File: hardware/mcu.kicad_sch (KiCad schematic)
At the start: 38 parts, among them J1 USB-C, SW3 RUN, SW4 BOOTSEL, U20 RP2350B, U21 W25Q128JVSIQ, U22 APS6404L-3SQR-SN, Y1 12MHz

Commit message: Hand-finish the last eight connections: fully routed, zero DRC errors
finish_route.py adds plane vias, clearance-checked stubs and single-layer
A* routing. Five signals run partly on the +3V3 plane layer (In2). SD_MISO
moves from GP36 to GP32 (both SPI0 RX) because the GP36 pad has no exit.
Schematic, GPIO table and README updated.

Co-Authored-By: Claude Fable 5.1 <noreply@anthropic.com>
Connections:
- net SD_MISO: now also U20.40 (GPIO32); no longer U20.45 (GPIO36)
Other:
- note added: "RP2350B core per the RP2350 hardware design guide. GPIO map: docs/v3-architecture.md section 7. GP31, GP33-GP36 spare."
- note removed: "RP2350B core per the RP2350 hardware design guide. GPIO map: docs/v3-architecture.md section 7. GP31-GP35 spare."
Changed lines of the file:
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@@
   (paper "A3")
   (title_block (title "TS-Pico v3: RP2350B Core") (rev "0.1") (company "Timex/Sinclair Online User Group"))
-  (text "RP2350B core per the RP2350 hardware design guide. GPIO map: docs/v3-architecture.md section 7. GP31-GP35 spare." (exclude_from_sim no) (at 20 285 0) (effects (font (size 2.5 2.5)) (justify left bottom)))
+  (text "RP2350B core per the RP2350 hardware design guide. GPIO map: docs/v3-architecture.md section 7. GP31, GP33-GP36 spare." (exclude_from_sim no) (at 20 285 0) (effects (font (size 2.5 2.5)) (justify left bottom)))
   (text "USB-C: data, and VBUS to the power sheet (diode-ORed with the edge +5V) so the card runs from USB alone on the bench." (exclude_from_sim no) (at 20 290 0) (effects (font (size 2.0 2.0)) (justify left bottom)))
   (symbol (lib_id "power:+3V3") (at 299.72 30.48 0) (unit 1)
@@
   (global_label "RESET_HOLD" (shape output) (at 154.94 175.26 0) (effects (font (size 1.27 1.27)) (justify left)))
   (global_label "AUDIO_R" (shape output) (at 154.94 177.80 0) (effects (font (size 1.27 1.27)) (justify left)))
-  (global_label "SD_MISO" (shape input) (at 154.94 193.04 0) (effects (font (size 1.27 1.27)) (justify left)))
+  (global_label "SD_MISO" (shape input) (at 154.94 182.88 0) (effects (font (size 1.27 1.27)) (justify left)))
   (global_label "SD_CS" (shape output) (at 154.94 195.58 0) (effects (font (size 1.27 1.27)) (justify left)))
   (global_label "SD_SCK" (shape output) (at 154.94 198.12 0) (effects (font (size 1.27 1.27)) (justify left)))
@@
   (global_label "AUDIO_L" (shape output) (at 104.14 198.12 180) (effects (font (size 1.27 1.27)) (justify right)))
   (no_connect (at 154.94 180.34))
-  (no_connect (at 154.94 182.88))
   (no_connect (at 154.94 185.42))
   (no_connect (at 154.94 187.96))
   (no_connect (at 154.94 190.50))
+  (no_connect (at 154.94 193.04))
   (label "PSRAM_CS" (at 104.14 200.66 180) (effects (font (size 1.27 1.27)) (justify right bottom)))
   (label "DVDD" (at 142.24 93.98 90) (effects (font (size 1.27 1.27)) (justify left bottom)))

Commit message: BOM cost optimisation against the JLCPCB catalog; schematic-side regulator fix
jlc_price.py prices the BOM via JLCPCB's parts API. Substitutions cut parts+fees
per board from $32.95 to $17.19 on a 10-board run: PSRAM DNP, electrolytic bulk
caps, TF-01A socket, PJ-320D jack, 74HC574, GD25Q128E, 0603 10 uF, basic LED,
preferred MCP6002; U16 decoder deleted (strobes on GPIO), U8 and U15 become
74LVC245s; J3/J5 hand-soldered. Adds the AOTA inductor and VREG_AVDD filter.
PCB needs a relayout; fab/ is stale.

Co-Authored-By: Claude Fable 5.1 <noreply@anthropic.com>
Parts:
- removed C34: 100n, Capacitor_SMD:C_0603_1608Metric, symbol Device:C
- added C39: 4.7u, Capacitor_SMD:C_0805_2012Metric, symbol Device:C
- added R28: 33, Resistor_SMD:R_0603_1608Metric, symbol Device:R
- L1: footprint Inductor_SMD:L_1008_2520Metric -> Inductor_SMD:L_0806_2016Metric; LCSC (none) -> C42411119; MPN SWPA252012S3R3MT -> AOTA-B201610S3R3-101-T
- U21: value W25Q128JVSIQ -> GD25Q128ESIGR; LCSC C97521 -> C2928891; MPN W25Q128JVSIQ -> GD25Q128ESIGR
- U22: now not fitted
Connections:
- net +3V3: now also R28.1; no longer U20.61 (VREG_AVDD)
- net DVDD: now also L1.1; no longer L1.2
- net GND: now also C39.2
- net VREG_LX: now also L1.2; no longer L1.1
- net nRD_STAT: now reaches U20.39 (GPIO31)
- net REG_SEL0 renamed nWR_ALO
- net REG_SEL1 renamed nWR_AHI
- net nREG_STB renamed nWR_CTL
- new net VREG_AVDD: C39.1, R28.2, U20.61 (VREG_AVDD)
- no-connect marks 7 -> 6
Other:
- note added: "C23-C33: one per IOVDD, QSPI_IOVDD, USB_OTP_VDD, ADC_AVDD pin, placed at the pin."
- note added: "L1 (Abracon AOTA-B201610S3R3-101-T, polarised: dot/pin 1 to DVDD)/C20/C21: RP2350 1.1 V core regulator. C22 at VREG_VIN."
- note added: "R28/C39: 33 R + 4.7 uF filter on VREG_AVDD (design guide R3/C9)."
- note added: "RP2350B core per the RP2350 hardware design guide. GPIO map: docs/v3-architecture.md section 7. GP33-GP36 spare."
- note added: "U21 boot flash (XIP CS0). U22 PSRAM on the same QSPI bus, DNP on the prototype ($5 part, SD-image cache only),"
- note removed: "C23-C34: one per IOVDD, QSPI_IOVDD, USB_OTP_VDD, ADC_AVDD, VREG_AVDD pin, placed at the pin."
- note removed: "L1/C20/C21: RP2350 internal 1.1 V core regulator. C22 at VREG_VIN."
- note removed: "RP2350B core per the RP2350 hardware design guide. GPIO map: docs/v3-architecture.md section 7. GP31, GP33-GP36 spare."
- note removed: "U21 boot flash (XIP CS0). U22 PSRAM on the same QSPI bus,"

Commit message: Logic consolidation: 15 packages to 8 fitted
Address buffers' output enables replace the 74LVC257 byte muxes and the MA bus;
one 74LVC32 makes MEMRD/MEMWR/IORD/IOWR strobes (replaces the 04 and 08);
XL9555 I2C expander replaces the CTL register, its power-on clear and the STAT
buffer; DMA parts are a DNP stuffing option (config.DMA_OPTION), with 74LVC574
latches directly on the address bus. GPIO map, architecture doc and cost notes
updated. Parts + fees per board now $14.93 on a 10-board run.

Co-Authored-By: Claude Fable 5.1 <noreply@anthropic.com>
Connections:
- net nRD_STAT is gone; now on net nWR_AHI: U20.39 (GPIO31)
- net nWR_CTL is gone; now on net nWR_ALO: U20.27 (GPIO26)
- net nWR_AHI: no longer U20.26 (GPIO25)
- net nWR_ALO: no longer U20.25 (GPIO24)
- net nDMA_EN: now reaches U20.42 (GPIO33)
- net nDMA_MREQ: now reaches U20.43 (GPIO34)
- net nIOX_INT: now reaches U20.44 (GPIO35)
- net ASEL renamed nAEN_X
- net nAOE renamed nAEN_Y
- net nIORQ_V renamed nMEMWR
- net nMREQ_V renamed nMEMRD
- net nRD_L renamed nIORD
- net nWR_L renamed nIOWR
- new net I2C_SCL: U20.26 (GPIO25)
- new net I2C_SDA: U20.25 (GPIO24)
- no-connect marks 6 -> 3
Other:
- note added: "RP2350B core per the RP2350 hardware design guide. GPIO map: docs/v3-architecture.md section 7. GP36 spare (plus the six DMA pins when the DMA option is off)."
- note removed: "RP2350B core per the RP2350 hardware design guide. GPIO map: docs/v3-architecture.md section 7. GP33-GP36 spare."
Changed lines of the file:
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@@
   (paper "A3")
   (title_block (title "TS-Pico v3: RP2350B Core") (rev "0.1") (company "Timex/Sinclair Online User Group"))
-  (text "RP2350B core per the RP2350 hardware design guide. GPIO map: docs/v3-architecture.md section 7. GP33-GP36 spare." (exclude_from_sim no) (at 20 285 0) (effects (font (size 2.5 2.5)) (justify left bottom)))
+  (text "RP2350B core per the RP2350 hardware design guide. GPIO map: docs/v3-architecture.md section 7. GP36 spare (plus the six DMA pins when the DMA option is off)." (exclude_from_sim no) (at 20 285 0) (effects (font (size 2.5 2.5)) (justify left bottom)))
   (text "USB-C: data, and VBUS to the power sheet (diode-ORed with the edge +5V) so the card runs from USB alone on the bench." (exclude_from_sim no) (at 20 290 0) (effects (font (size 2.0 2.0)) (justify left bottom)))
   (symbol (lib_id "power:+3V3") (at 299.72 30.48 0) (unit 1)
@@
   (global_label "MD6" (shape bidirectional) (at 154.94 116.84 0) (effects (font (size 1.27 1.27)) (justify left)))
   (global_label "MD7" (shape bidirectional) (at 154.94 119.38 0) (effects (font (size 1.27 1.27)) (justify left)))
-  (global_label "ASEL" (shape output) (at 154.94 121.92 0) (effects (font (size 1.27 1.27)) (justify left)))
-  (global_label "nAOE" (shape output) (at 154.94 124.46 0) (effects (font (size 1.27 1.27)) (justify left)))
+  (global_label "nAEN_X" (shape output) (at 154.94 121.92 0) (effects (font (size 1.27 1.27)) (justify left)))
+  (global_label "nAEN_Y" (shape output) (at 154.94 124.46 0) (effects (font (size 1.27 1.27)) (justify left)))
   (global_label "nDATA_OE" (shape output) (at 154.94 127.00 0) (effects (font (size 1.27 1.27)) (justify left)))
   (global_label "BE_REQ" (shape output) (at 154.94 129.54 0) (effects (font (size 1.27 1.27)) (justify left)))
@@
   (global_label "Z80_A14" (shape input) (at 154.94 134.62 0) (effects (font (size 1.27 1.27)) (justify left)))
   (global_label "Z80_A15" (shape input) (at 154.94 137.16 0) (effects (font (size 1.27 1.27)) (justify left)))
-  (global_label "nMREQ_V" (shape input) (at 154.94 139.70 0) (effects (font (size 1.27 1.27)) (justify left)))
-  (global_label "nIORQ_V" (shape input) (at 154.94 142.24 0) (effects (font (size 1.27 1.27)) (justify left)))
-  (global_label "nRD_L" (shape input) (at 154.94 144.78 0) (effects (font (size 1.27 1.27)) (justify left)))
-  (global_label "nWR_L" (shape input) (at 154.94 147.32 0) (effects (font (size 1.27 1.27)) (justify left)))
+  (global_label "nMEMRD" (shape input) (at 154.94 139.70 0) (effects (font (size 1.27 1.27)) (justify left)))
+  (global_label "nMEMWR" (shape input) (at 154.94 142.24 0) (effects (font (size 1.27 1.27)) (justify left)))
+  (global_label "nIORD" (shape input) (at 154.94 144.78 0) (effects (font (size 1.27 1.27)) (justify left)))
+  (global_label "nIOWR" (shape input) (at 154.94 147.32 0) (effects (font (size 1.27 1.27)) (justify left)))
   (global_label "nROSCS_L" (shape input) (at 154.94 149.86 0) (effects (font (size 1.27 1.27)) (justify left)))
   (global_label "nEXROM_L" (shape input) (at 154.94 152.40 0) (effects (font (size 1.27 1.27)) (justify left)))
@@
   (global_label "TAPE_IN" (shape input) (at 154.94 157.48 0) (effects (font (size 1.27 1.27)) (justify left)))
   (global_label "TAPE_OUT" (shape output) (at 154.94 160.02 0) (effects (font (size 1.27 1.27)) (justify left)))
-  (global_label "nWR_ALO" (shape output) (at 154.94 162.56 0) (effects (font (size 1.27 1.27)) (justify left)))
-  (global_label "nWR_AHI" (shape output) (at 154.94 165.10 0) (effects (font (size 1.27 1.27)) (justify left)))
-  (global_label "nWR_CTL" (shape output) (at 154.94 167.64 0) (effects (font (size 1.27 1.27)) (justify left)))
-  (global_label "nRD_STAT" (shape output) (at 154.94 180.34 0) (effects (font (size 1.27 1.27)) (justify left)))
-  (global_label "nMRD" (shape output) (at 154.94 170.18 0) (effects (font (size 1.27 1.27)) (justify left)))
-  (global_label "nMWR" (shape output) (at 154.94 172.72 0) (effects (font (size 1.27 1.27)) (justify left)))
+  (global_label "I2C_SDA" (shape bidirectional) (at 154.94 162.56 0) (effects (font (size 1.27 1.27)) (justify left)))
+  (global_label "I2C_SCL" (shape output) (at 154.94 165.10 0) (effects (font (size 1.27 1.27)) (justify left)))
   (global_label "RESET_HOLD" (shape output) (at 154.94 175.26 0) (effects (font (size 1.27 1.27)) (justify left)))
   (global_label "AUDIO_R" (shape output) (at 154.94 177.80 0) (effects (font (size 1.27 1.27)) (justify left)))
   (global_label "SD_MISO" (shape input) (at 154.94 182.88 0) (effects (font (size 1.27 1.27)) (justify left)))
+  (global_label "nIOX_INT" (shape input) (at 154.94 190.50 0) (effects (font (size 1.27 1.27)) (justify left)))
   (global_label "SD_CS" (shape output) (at 154.94 195.58 0) (effects (font (size 1.27 1.27)) (justify left)))
   (global_label "SD_SCK" (shape output) (at 154.94 198.12 0) (effects (font (size 1.27 1.27)) (justify left)))
@@
   (global_label "WIFI_RX" (shape input) (at 104.14 195.58 180) (effects (font (size 1.27 1.27)) (justify right)))
   (global_label "AUDIO_L" (shape output) (at 104.14 198.12 180) (effects (font (size 1.27 1.27)) (justify right)))
-  (no_connect (at 154.94 185.42))
-  (no_connect (at 154.94 187.96))
-  (no_connect (at 154.94 190.50))
+  (global_label "nWR_ALO" (shape output) (at 154.94 167.64 0) (effects (font (size 1.27 1.27)) (justify left)))
+  (global_label "nMRD" (shape output) (at 154.94 170.18 0) (effects (font (size 1.27 1.27)) (justify left)))
+  (global_label "nMWR" (shape output) (at 154.94 172.72 0) (effects (font (size 1.27 1.27)) (justify left)))
+  (global_label "nWR_AHI" (shape output) (at 154.94 180.34 0) (effects (font (size 1.27 1.27)) (justify left)))
+  (global_label "nDMA_EN" (shape output) (at 154.94 185.42 0) (effects (font (size 1.27 1.27)) (justify left)))
+  (global_label "nDMA_MREQ" (shape output) (at 154.94 187.96 0) (effects (font (size 1.27 1.27)) (justify left)))
   (no_connect (at 154.94 193.04))
   (label "PSRAM_CS" (at 104.14 200.66 180) (effects (font (size 1.27 1.27)) (justify right bottom)))

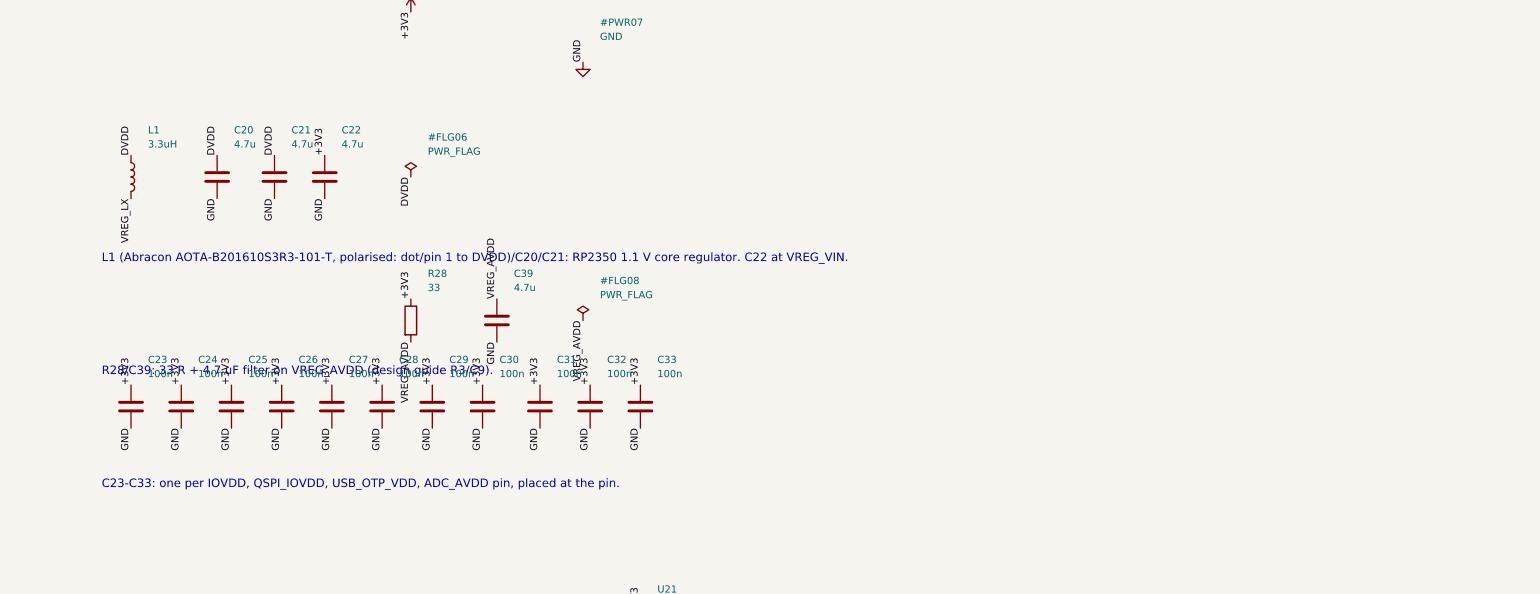
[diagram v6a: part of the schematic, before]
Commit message: Relayout: 130 x 64.25 mm board with the consolidated logic and cheaper BOM
Regulator and crystal hand-routed per the RP2350 design guide (locked
pre-routes), TF-01A socket flush with the edge, custom footprints from LCSC
land patterns, 0.15 mm signal tracks, 0.6/0.3 vias throughout. New flow:
gen_layout -> preroute -> autoroute -> finish. Zero DRC violations; open are
two nets of the unfitted DMA option (nMRD, nWR_ALO). Fab outputs regenerated.

Co-Authored-By: Claude Fable 5.1 <noreply@anthropic.com>
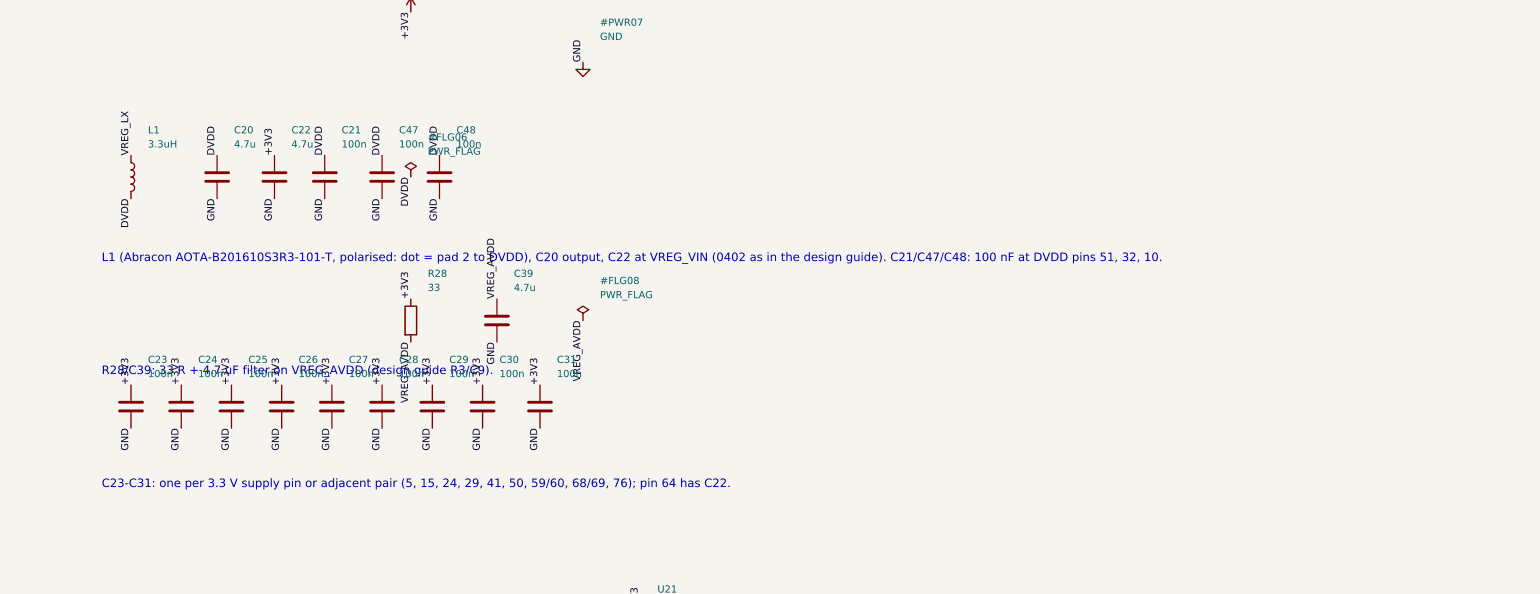
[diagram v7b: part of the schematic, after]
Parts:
- removed C32, C33: 100n, Capacitor_SMD:C_0603_1608Metric, symbol Device:C
- added C47, C48: 100n, Capacitor_SMD:C_0603_1608Metric, symbol Device:C
- C20, C22, C39: footprint Capacitor_SMD:C_0805_2012Metric -> Capacitor_SMD:C_0402_1005Metric; LCSC C1779 -> C23733; MPN CL21A475KAQNNNE -> CL05A475MP5NRNC
- C21: value 4.7u -> 100n; footprint Capacitor_SMD:C_0805_2012Metric -> Capacitor_SMD:C_0603_1608Metric; LCSC C1779 -> C14663; MPN CL21A475KAQNNNE -> CC0603KRX7R9BB104
- L1: footprint Inductor_SMD:L_0806_2016Metric -> tspico:L_Abracon_AOTA-B201610
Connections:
- net DVDD: now also L1.2, C47.1, C48.1; no longer L1.1
- net GND: now also C47.2, C48.2
- net VREG_LX: now also L1.1; no longer L1.2
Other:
- note added: "C23-C31: one per 3.3 V supply pin or adjacent pair (5, 15, 24, 29, 41, 50, 59/60, 68/69, 76); pin 64 has C22."
- note added: "L1 (Abracon AOTA-B201610S3R3-101-T, polarised: dot = pad 2 to DVDD), C20 output, C22 at VREG_VIN (0402 as in the design guide). C21/C47/C48: 100 nF at DVDD pins 51, 32, 10."
- note removed: "C23-C33: one per IOVDD, QSPI_IOVDD, USB_OTP_VDD, ADC_AVDD pin, placed at the pin."
- note removed: "L1 (Abracon AOTA-B201610S3R3-101-T, polarised: dot/pin 1 to DVDD)/C20/C21: RP2350 1.1 V core regulator. C22 at VREG_VIN."

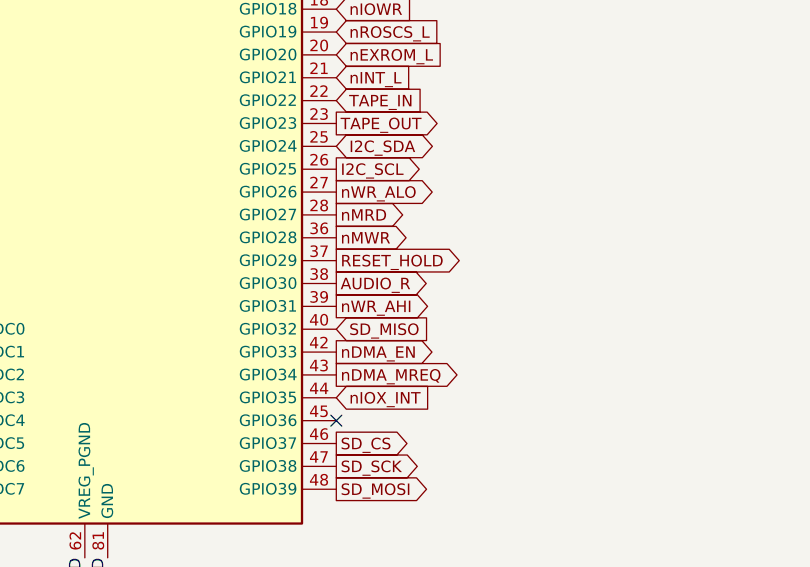
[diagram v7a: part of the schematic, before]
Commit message: Drop the DMA option: board fully routed, zero DRC errors
DMA_OPTION = False removes U8, U9, U12, U13 and six GPIOs; the data transceiver
takes DIR from /RD with its A side on the Z80 bus. Rerouted with the scripted
flow; finish order is DVDD before +3V3, supply pin 29 escapes through the freed
pad lanes, DVDD widened to 0.25 mm. No signal on either plane layer, all vias
0.6/0.3. Fab outputs regenerated; parts + fees $14.48 per board at 10 boards.

Co-Authored-By: Claude Fable 5.1 <noreply@anthropic.com>
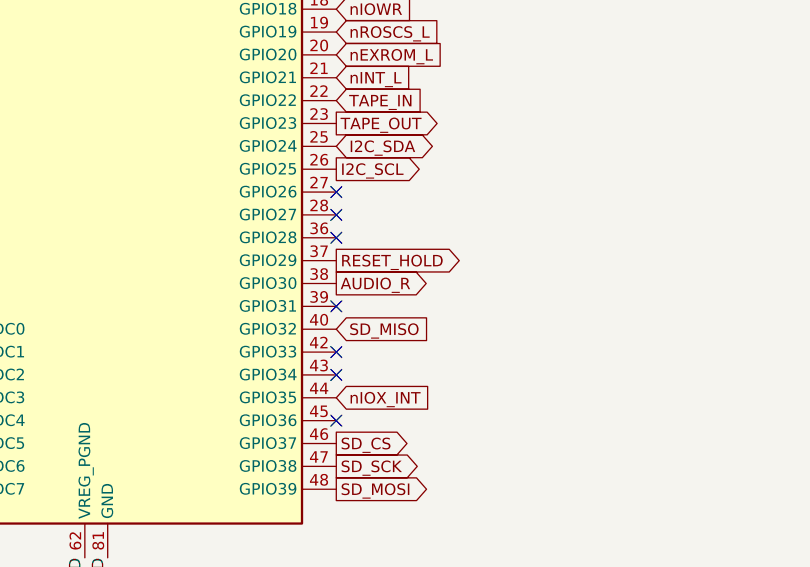
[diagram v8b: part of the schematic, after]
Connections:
- net nDMA_EN: no longer names the net of U20.42 (GPIO33)
- net nDMA_MREQ: no longer names the net of U20.43 (GPIO34)
- net nMRD: no longer names the net of U20.28 (GPIO27)
- net nMWR: no longer names the net of U20.36 (GPIO28)
- net nWR_AHI: no longer names the net of U20.39 (GPIO31)
- net nWR_ALO: no longer names the net of U20.27 (GPIO26)
- no-connect marks 3 -> 9
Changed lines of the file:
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@@
   (global_label "WIFI_RX" (shape input) (at 104.14 195.58 180) (effects (font (size 1.27 1.27)) (justify right)))
   (global_label "AUDIO_L" (shape output) (at 104.14 198.12 180) (effects (font (size 1.27 1.27)) (justify right)))
-  (global_label "nWR_ALO" (shape output) (at 154.94 167.64 0) (effects (font (size 1.27 1.27)) (justify left)))
-  (global_label "nMRD" (shape output) (at 154.94 170.18 0) (effects (font (size 1.27 1.27)) (justify left)))
-  (global_label "nMWR" (shape output) (at 154.94 172.72 0) (effects (font (size 1.27 1.27)) (justify left)))
-  (global_label "nWR_AHI" (shape output) (at 154.94 180.34 0) (effects (font (size 1.27 1.27)) (justify left)))
-  (global_label "nDMA_EN" (shape output) (at 154.94 185.42 0) (effects (font (size 1.27 1.27)) (justify left)))
-  (global_label "nDMA_MREQ" (shape output) (at 154.94 187.96 0) (effects (font (size 1.27 1.27)) (justify left)))
   (no_connect (at 154.94 193.04))
+  (no_connect (at 154.94 167.64))
+  (no_connect (at 154.94 170.18))
+  (no_connect (at 154.94 172.72))
+  (no_connect (at 154.94 180.34))
+  (no_connect (at 154.94 185.42))
+  (no_connect (at 154.94 187.96))
   (label "PSRAM_CS" (at 104.14 200.66 180) (effects (font (size 1.27 1.27)) (justify right bottom)))
   (label "DVDD" (at 142.24 93.98 90) (effects (font (size 1.27 1.27)) (justify left bottom)))
